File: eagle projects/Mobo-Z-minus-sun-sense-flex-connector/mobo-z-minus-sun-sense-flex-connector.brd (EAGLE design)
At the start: 24.8 x 196.8 mm, 2 parts, among them X1 5X2_SMD_2.54MM_HEADER, X2 5X2_SMD_2.54MM_HEADER

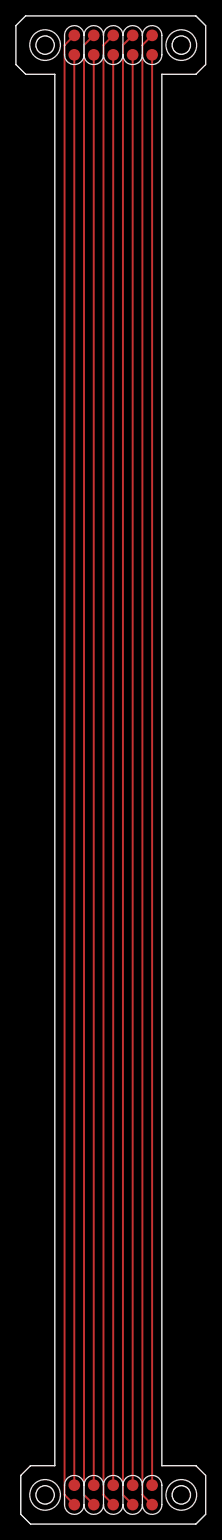
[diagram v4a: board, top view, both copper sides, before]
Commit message: Fixed Connector Boards
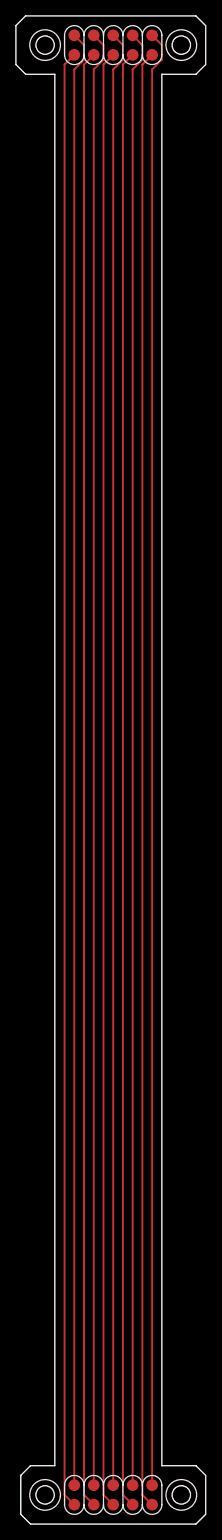
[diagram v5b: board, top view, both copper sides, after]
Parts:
- turned X2 to 180 degrees
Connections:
- net N$1: now also X2.P6; no longer X2.P10
- net N$10: now also X1.P1; no longer X1.P5
- net N$2: now also X2.P7; no longer X2.P9
- net N$4: now also X2.P9; no longer X2.P7
- net N$5: now also X2.P10; no longer X2.P6
- net N$6: now also X1.P5; no longer X1.P1
- net N$7: now also X1.P4; no longer X1.P2
- net N$9: now also X1.P2; no longer X1.P4
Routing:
- net N$9: track 186.7 -> 190.9 mm
- net N$8: track 186.7 -> 190.3 mm
- net N$7: track 186.7 -> 190.3 mm
- net N$6: track 186.7 -> 190.3 mm
- net N$10: track 186.7 -> 190.3 mm
- net N$5: track 192.8 -> 190.3 mm
- net N$4: track 192.8 -> 190.3 mm
- net N$3: track 192.8 -> 190.3 mm
- net N$2: track 192.8 -> 190.3 mm
- net N$1: track 192.8 -> 190.3 mm
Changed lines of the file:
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@@
 <elements>
 <element name="X1" library="SMD_headers" package="5X2_HEADER" value="5X2_SMD_2.54MM_HEADER" x="10.16" y="189.23" smashed="yes" rot="R180"/>
-<element name="X2" library="SMD_headers" package="5X2_HEADER" value="5X2_SMD_2.54MM_HEADER" x="10.16" y="0" smashed="yes"/>
+<element name="X2" library="SMD_headers" package="5X2_HEADER" value="5X2_SMD_2.54MM_HEADER" x="10.16" y="0" smashed="yes" rot="R180"/>
 </elements>
 <signals>
+<signal name="N$1">
+<contactref element="X2" pad="P6"/>
+<contactref element="X1" pad="P6"/>
+<wire x1="5.08" y1="1.27" x2="5.08" y2="186.055" width="0.254" layer="1"/>
+<wire x1="5.08" y1="186.055" x2="6.35" y2="187.325" width="0.254" layer="1"/>
+<wire x1="6.35" y1="187.325" x2="6.35" y2="189.23" width="0.254" layer="1"/>
+<wire x1="6.35" y1="189.23" x2="5.08" y2="190.5" width="0.254" layer="1"/>
+</signal>
+<signal name="N$2">
+<contactref element="X2" pad="P7"/>
+<contactref element="X1" pad="P7"/>
+<wire x1="7.62" y1="1.27" x2="7.62" y2="186.055" width="0.254" layer="1"/>
+<wire x1="7.62" y1="186.055" x2="8.89" y2="187.325" width="0.254" layer="1"/>
+<wire x1="8.89" y1="187.325" x2="8.89" y2="189.23" width="0.254" layer="1"/>
+<wire x1="8.89" y1="189.23" x2="7.62" y2="190.5" width="0.254" layer="1"/>
+</signal>
+<signal name="N$3">
+<contactref element="X2" pad="P8"/>
+<contactref element="X1" pad="P8"/>
+<wire x1="10.16" y1="1.27" x2="10.16" y2="186.055" width="0.254" layer="1"/>
+<wire x1="10.16" y1="186.055" x2="11.43" y2="187.325" width="0.254" layer="1"/>
+<wire x1="11.43" y1="187.325" x2="11.43" y2="189.23" width="0.254" layer="1"/>
+<wire x1="11.43" y1="189.23" x2="10.16" y2="190.5" width="0.254" layer="1"/>
+</signal>
+<signal name="N$4">
+<contactref element="X2" pad="P9"/>
+<contactref element="X1" pad="P9"/>
+<wire x1="12.7" y1="1.27" x2="12.7" y2="186.055" width="0.254" layer="1"/>
+<wire x1="12.7" y1="186.055" x2="13.97" y2="187.325" width="0.254" layer="1"/>
+<wire x1="13.97" y1="187.325" x2="13.97" y2="189.23" width="0.254" layer="1"/>
+<wire x1="13.97" y1="189.23" x2="12.7" y2="190.5" width="0.254" layer="1"/>
+</signal>
+<signal name="N$5">
+<contactref element="X2" pad="P10"/>
+<contactref element="X1" pad="P10"/>
+<wire x1="15.24" y1="1.27" x2="15.24" y2="186.055" width="0.254" layer="1"/>
+<wire x1="15.24" y1="186.055" x2="16.51" y2="187.325" width="0.254" layer="1"/>
+<wire x1="16.51" y1="187.325" x2="16.51" y2="189.23" width="0.254" layer="1"/>
+<wire x1="16.51" y1="189.23" x2="15.24" y2="190.5" width="0.254" layer="1"/>
+</signal>
 <signal name="N$6">
-<contactref element="X1" pad="P1"/>
 <contactref element="X2" pad="P5"/>
-<wire x1="5.08" y1="1.27" x2="5.08" y2="187.96" width="0.254" layer="1"/>
+<contactref element="X1" pad="P5"/>
+<wire x1="15.24" y1="187.96" x2="13.97" y2="186.69" width="0.254" layer="1"/>
+<wire x1="13.97" y1="186.69" x2="13.97" y2="0" width="0.254" layer="1"/>
+<wire x1="13.97" y1="0" x2="15.24" y2="-1.27" width="0.254" layer="1"/>
 </signal>
 <signal name="N$7">
-<contactref element="X1" pad="P2"/>
+<contactref element="X1" pad="P4"/>
 <contactref element="X2" pad="P4"/>
-<wire x1="7.62" y1="187.96" x2="7.62" y2="1.27" width="0.254" layer="1"/>
+<wire x1="12.7" y1="187.96" x2="11.43" y2="186.69" width="0.254" layer="1"/>
+<wire x1="11.43" y1="186.69" x2="11.43" y2="0" width="0.254" layer="1"/>
+<wire x1="11.43" y1="0" x2="12.7" y2="-1.27" width="0.254" layer="1"/>
 </signal>
 <signal name="N$8">
+<contactref element="X2" pad="P3"/>
 <contactref element="X1" pad="P3"/>
-<contactref element="X2" pad="P3"/>
-<wire x1="10.16" y1="1.27" x2="10.16" y2="187.96" width="0.254" layer="1"/>
+<wire x1="10.16" y1="187.96" x2="8.89" y2="186.69" width="0.254" layer="1"/>
+<wire x1="8.89" y1="186.69" x2="8.89" y2="0" width="0.254" layer="1"/>
+<wire x1="8.89" y1="0" x2="10.16" y2="-1.27" width="0.254" layer="1"/>
 </signal>
 <signal name="N$9">
-<contactref element="X1" pad="P4"/>
+<contactref element="X1" pad="P2"/>
 <contactref element="X2" pad="P2"/>
-<wire x1="12.7" y1="187.96" x2="12.7" y2="1.27" width="0.254" layer="1"/>
+<wire x1="7.62" y1="187.96" x2="7.62" y2="187.325" width="0.254" layer="1"/>
+<wire x1="6.35" y1="186.055" x2="6.35" y2="185.42" width="0.254" layer="1"/>
+<wire x1="6.35" y1="185.42" x2="6.35" y2="0" width="0.254" layer="1"/>
+<wire x1="6.35" y1="0" x2="7.62" y2="-1.27" width="0.254" layer="1"/>
+<wire x1="7.62" y1="187.96" x2="6.35" y2="186.69" width="0.254" layer="1"/>
+<wire x1="6.35" y1="186.69" x2="6.35" y2="186.055" width="0.254" layer="1"/>
 </signal>
 <signal name="N$10">
-<contactref element="X1" pad="P5"/>
 <contactref element="X2" pad="P1"/>
-<wire x1="15.24" y1="187.96" x2="15.24" y2="1.27" width="0.254" layer="1"/>
-</signal>
-<signal name="N$1">
-<contactref element="X1" pad="P6"/>
-<contactref element="X2" pad="P10"/>
-<wire x1="3.81" y1="0" x2="5.08" y2="-1.27" width="0.254" layer="1"/>
-<wire x1="5.08" y1="190.5" x2="3.81" y2="189.23" width="0.254" layer="1"/>
-<wire x1="3.81" y1="189.23" x2="3.81" y2="0" width="0.254" layer="1"/>
-</signal>
-<signal name="N$2">
-<contactref element="X1" pad="P7"/>
-<contactref element="X2" pad="P9"/>
-<wire x1="6.35" y1="189.23" x2="7.62" y2="190.5" width="0.254" layer="1"/>
-<wire x1="7.62" y1="-1.27" x2="6.35" y2="0" width="0.254" layer="1"/>
-<wire x1="6.35" y1="0" x2="6.35" y2="189.23" width="0.254" layer="1"/>
-</signal>
-<signal name="N$3">
-<contactref element="X1" pad="P8"/>
-<contactref element="X2" pad="P8"/>
-<wire x1="8.89" y1="0" x2="10.16" y2="-1.27" width="0.254" layer="1"/>
-<wire x1="10.16" y1="190.5" x2="8.89" y2="189.23" width="0.254" layer="1"/>
-<wire x1="8.89" y1="189.23" x2="8.89" y2="0" width="0.254" layer="1"/>
-</signal>
-<signal name="N$4">
-<contactref element="X1" pad="P9"/>
-<contactref element="X2" pad="P7"/>
-<wire x1="11.43" y1="189.23" x2="12.7" y2="190.5" width="0.254" layer="1"/>
-<wire x1="12.7" y1="-1.27" x2="11.43" y2="0" width="0.254" layer="1"/>
-<wire x1="11.43" y1="0" x2="11.43" y2="189.23" width="0.254" layer="1"/>
-</signal>
-<signal name="N$5">
-<contactref element="X1" pad="P10"/>
-<contactref element="X2" pad="P6"/>
-<wire x1="13.97" y1="0" x2="15.24" y2="-1.27" width="0.254" layer="1"/>
-<wire x1="15.24" y1="190.5" x2="13.97" y2="189.23" width="0.254" layer="1"/>
-<wire x1="13.97" y1="189.23" x2="13.97" y2="0" width="0.254" layer="1"/>
+<contactref element="X1" pad="P1"/>
+<wire x1="5.08" y1="-1.27" x2="3.81" y2="0" width="0.254" layer="1"/>
+<wire x1="3.81" y1="186.69" x2="5.08" y2="187.96" width="0.254" layer="1"/>
+<wire x1="3.81" y1="0" x2="3.81" y2="186.69" width="0.254" layer="1"/>
 </signal>
 </signals>
